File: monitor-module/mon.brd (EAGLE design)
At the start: 50 x 24 mm, 11 parts

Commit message: submitted
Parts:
- moved U$2 1.02 mm to (20.6, 17.0)
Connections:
- new net N$3: U$1.6, U$2.DIO0
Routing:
- net MOSI: track 10.3 -> 53.6 mm, vias 0 -> 1
- net MISO: track 0.00 -> 43.2 mm, vias 0 -> 1
- net SCK: track 4.43 -> 46.1 mm, vias 0 -> 1
- net RFM_CS: track 0.00 -> 35.9 mm, vias 0 -> 1
- net N$3: track 0.00 -> 14.6 mm, vias 0 -> 1
- net VCC: track 67.8 -> 77.2 mm
- net DISPLAY_DC: track 17.2 -> 20.8 mm
- net DISPLAY_CS: track 12.1 -> 15.2 mm
- net UART_TX: track 20.8 -> 21.8 mm
- net N$1: track 7.16 -> 8.18 mm
- net UART_RX: track 31.5 -> 32.3 mm
- net SWDAT: track 13.7 -> 13.0 mm
- net GND: vias 0 -> 39
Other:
- board text added: "CLK"
- board text added: "CS"
- board text added: "DC"
- board text added: "ESP"
- board text added: "GND"
- board text added: "MOSI"
- board text added: "VCC"
- board text removed: "ESP8266"

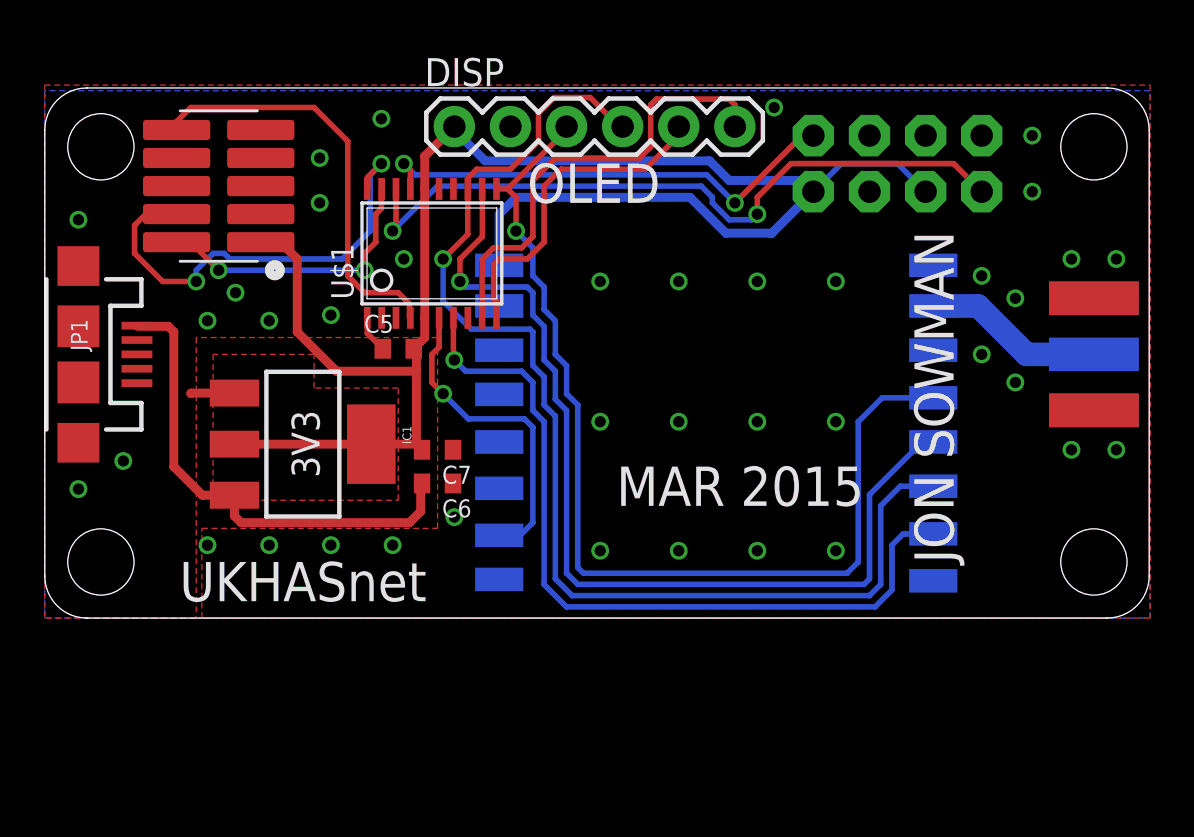
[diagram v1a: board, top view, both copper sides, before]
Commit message: added jumpers because dont trust ebay sellers
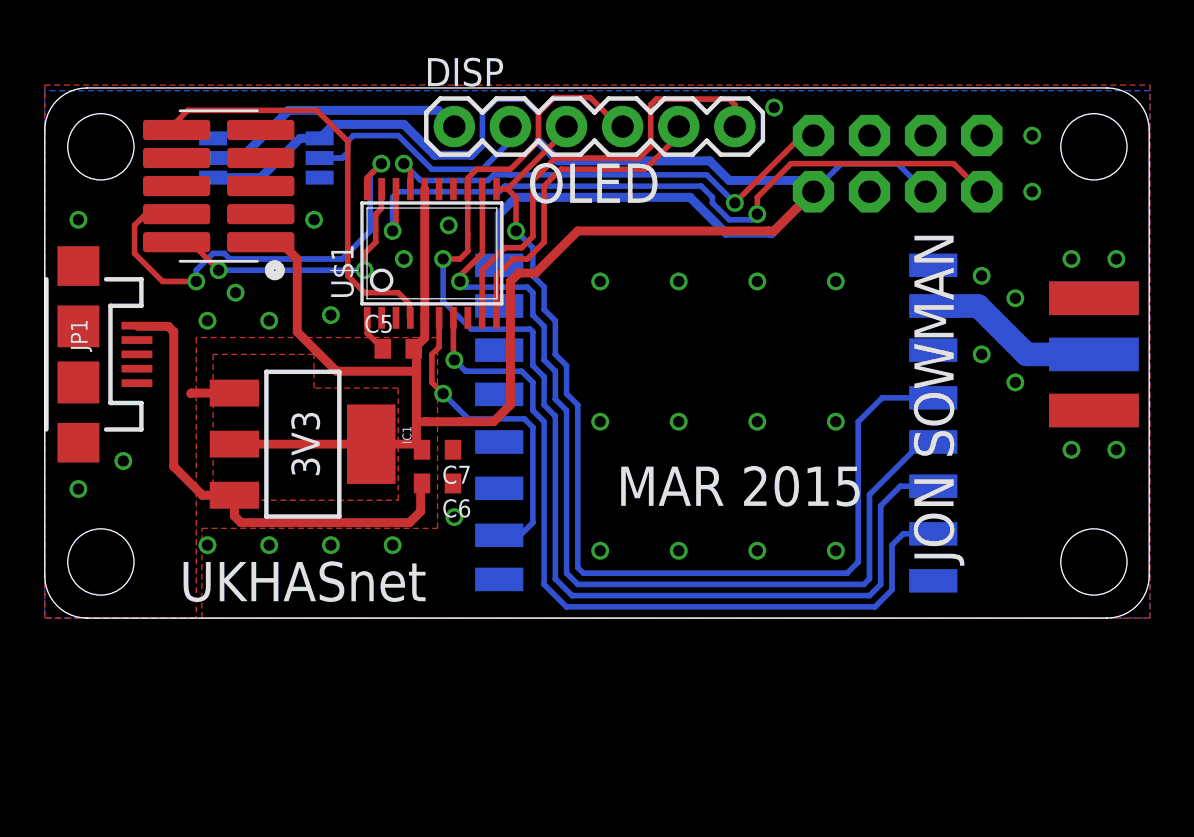
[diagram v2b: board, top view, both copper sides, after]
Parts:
- added SJ1, SJ2: (no value), SparkFun-Retired:SJ_3
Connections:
- new net N$4: DISP.2, SJ1.2
- new net N$5: DISP.1, SJ2.2
- net GND: now also SJ1.3, SJ2.3; no longer DISP.2
- net VCC: now also SJ1.1, SJ2.1; no longer DISP.1
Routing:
- net VCC: track 77.2 -> 115.0 mm
- net N$5: track 0.00 -> 12.1 mm
- net N$4: track 0.00 -> 11.2 mm
- net UART_RX: track 32.3 -> 33.2 mm
- net GND: vias 39 -> 38
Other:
- board text added: "+"
- board text added: "P1"
- board text added: "P2"
